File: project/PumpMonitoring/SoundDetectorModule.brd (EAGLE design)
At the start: 46 x 22 mm, 32 parts, among them CN1 JST-PH-K*, IC1 LMV324

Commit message: modify schematic of sound detect module.
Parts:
- added C5, C6: NC, SparkFun-Capacitors:1206
- added R22: NC, SparkFun-Resistors:0603-RES
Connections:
- new net N$13: C5.2
- net GND: now also C5.1, C6.1
- net N$2: now also C6.2, R22.2
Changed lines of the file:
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@@
 <?xml version="1.0" encoding="utf-8"?>
 <!DOCTYPE eagle SYSTEM "eagle.dtd">
-<eagle version="7.7.0">
+<eagle version="7.6.0">
 <drawing>
 <settings>
@@
 <layer number="21" name="tPlace" color="7" fill="1" visible="yes" active="yes"/>
 <layer number="22" name="bPlace" color="7" fill="1" visible="yes" active="yes"/>
-<layer number="23" name="tOrigins" color="15" fill="1" visible="no" active="yes"/>
-<layer number="24" name="bOrigins" color="15" fill="1" visible="no" active="yes"/>
+<layer number="23" name="tOrigins" color="15" fill="1" visible="yes" active="yes"/>
+<layer number="24" name="bOrigins" color="15" fill="1" visible="yes" active="yes"/>
 <layer number="25" name="tNames" color="7" fill="1" visible="no" active="yes"/>
 <layer number="26" name="bNames" color="7" fill="1" visible="no" active="yes"/>
@@
 <element name="R20" library="resistor" package="0207/7" value="0" x="12.319" y="6.731" rot="R180"/>
 <element name="R21" library="resistor" package="0207/7" value="0" x="30.226" y="6.858"/>
+<element name="C5" library="SparkFun-Capacitors" package="1206" value="NC" x="1.27" y="-3.81">
+<attribute name="PROD_ID" value="CAP-10057" x="1.27" y="-3.81" size="1.778" layer="27" display="off"/>
+</element>
+<element name="R22" library="SparkFun-Resistors" package="0603-RES" value="NC" x="1.27" y="-7.62">
+<attribute name="PROD_ID" value="RES-07856" x="1.27" y="-7.62" size="1.778" layer="27" display="off"/>
+</element>
+<element name="C6" library="SparkFun-Capacitors" package="1206" value="NC" x="1.27" y="-11.43">
+<attribute name="PROD_ID" value="CAP-10057" x="1.27" y="-11.43" size="1.778" layer="27" display="off"/>
+</element>
 </elements>
 <signals>
@@
 <wire x1="35.306" y1="13.973" x2="33.912" y2="15.367" width="0.2032" layer="1"/>
 <wire x1="33.912" y1="15.367" x2="33.147" y2="15.367" width="0.2032" layer="1"/>
+<contactref element="C5" pad="1"/>
+<contactref element="C6" pad="1"/>
+<wire x1="-0.13" y1="-3.81" x2="-0.13" y2="-11.43" width="0" layer="19" extent="1-1"/>
+<wire x1="7.461" y1="13.589" x2="-0.13" y2="-3.81" width="0" layer="19" extent="1-1"/>
 </signal>
 <signal name="N$2">
@@
 <wire x1="16.764" y1="9.525" x2="16.002" y2="8.763" width="0.2032" layer="1"/>
 <wire x1="16.002" y1="8.763" x2="12.7" y2="8.763" width="0.2032" layer="1"/>
+<contactref element="R22" pad="2"/>
+<contactref element="C6" pad="2"/>
+<wire x1="2.12" y1="-7.62" x2="12.7" y2="8.763" width="0" layer="19" extent="1-1"/>
+<wire x1="2.67" y1="-11.43" x2="2.12" y2="-7.62" width="0" layer="19" extent="1-1"/>
 </signal>
 <signal name="AUDIO">
@@
 <wire x1="21.883" y1="4.279" x2="20.701" y2="5.461" width="0.2032" layer="1"/>
 </signal>
+<signal name="N$13">
+<contactref element="C5" pad="2"/>
+</signal>
 </signals>

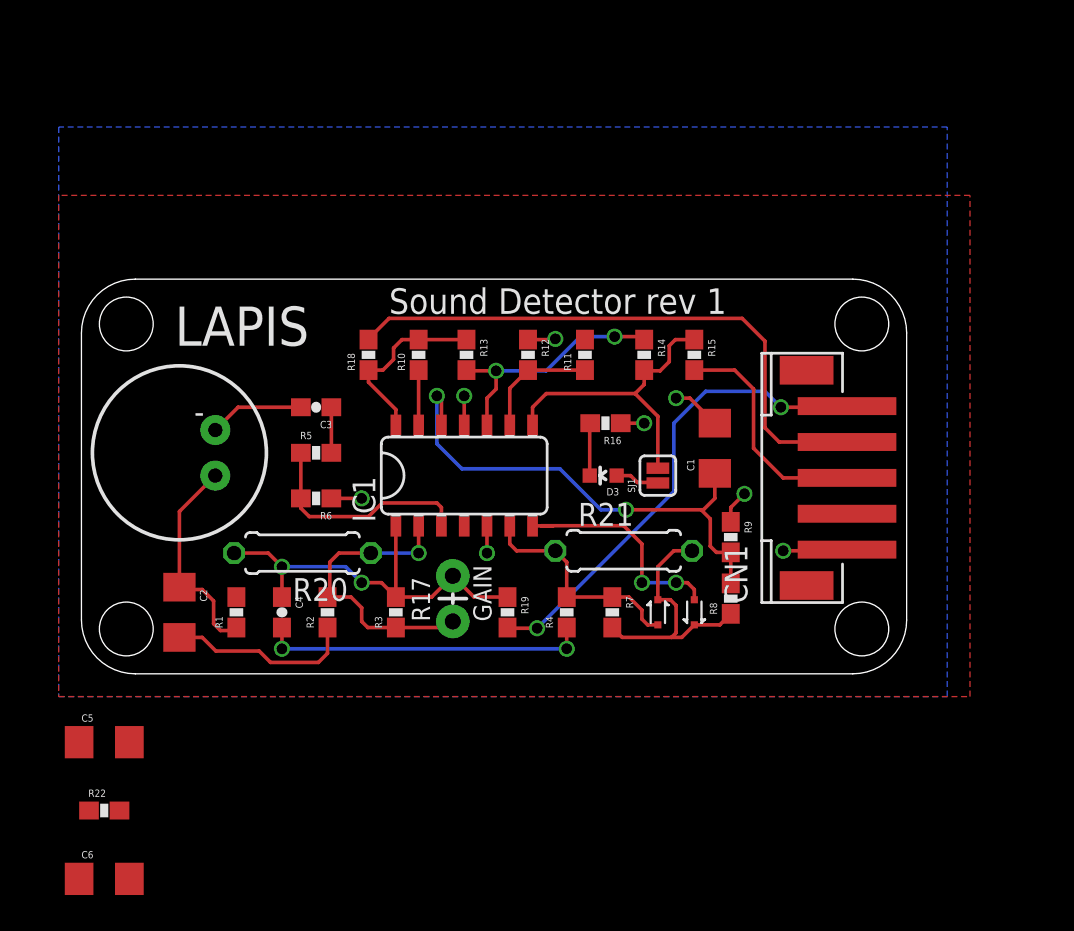
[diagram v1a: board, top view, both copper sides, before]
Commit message: update sound detector module
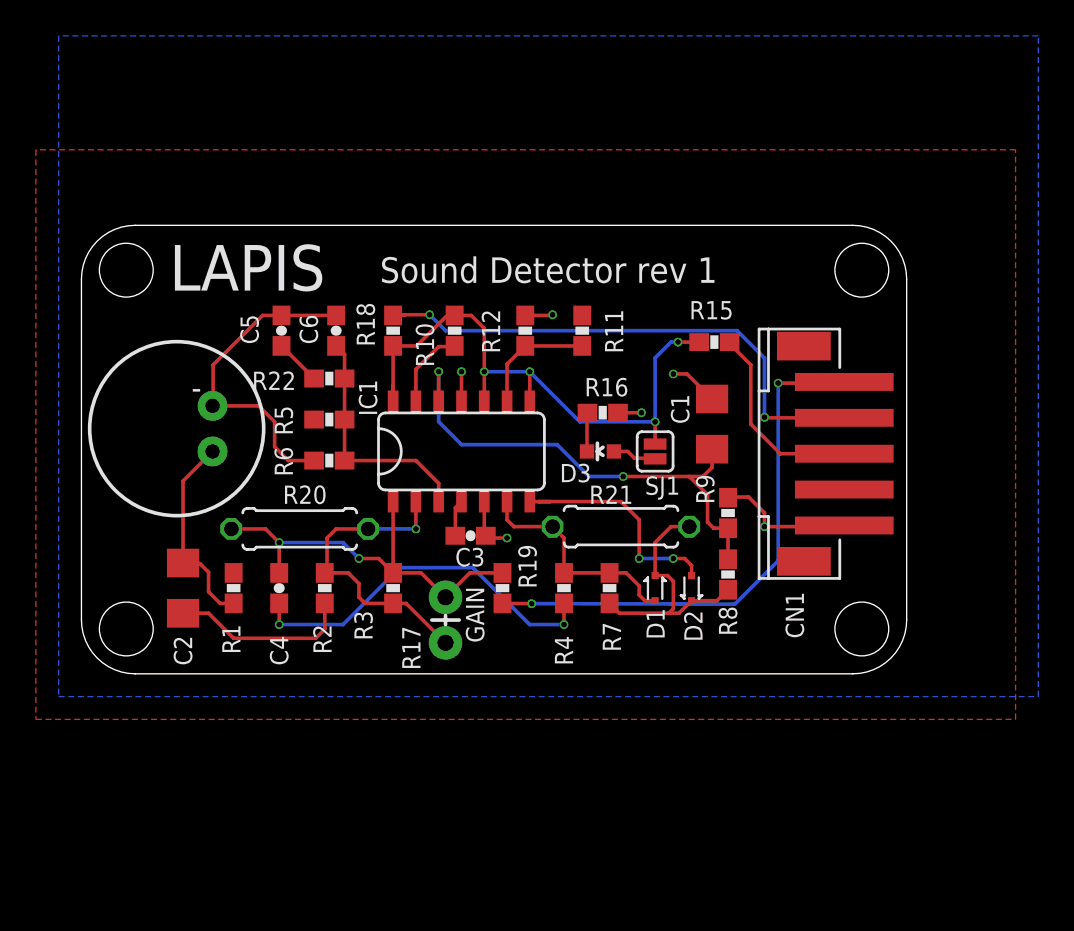
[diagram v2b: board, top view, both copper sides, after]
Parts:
- removed R13: 1K, SparkFun-Resistors:0603-RES
- removed R14: 100k, SparkFun-Resistors:0603-RES
- C5, C6: device SparkFun-Capacitors:1206 -> SparkFun-Capacitors:0603-CAP
- moved C6 33.2 mm to (14.2, 19.1), turned to 90 degrees
- moved R22 27.2 mm to (13.8, 16.5)
- moved C5 25.0 mm to (11.2, 19.1), turned to 270 degrees
- moved C3 11.2 mm to (21.7, 7.70), turned to 0 degrees
- moved R10 2.42 mm to (20.8, 19.1)
- moved R6 2.23 mm to (13.8, 11.9), turned to 0 degrees
- moved R5 2.00 mm to (13.8, 14.2), turned to 180 degrees
- moved R18 1.92 mm to (17.4, 19.1)
- moved R19 1.37 mm to (23.5, 4.78)
- moved C2 1.36 mm to (5.66, 4.78)
- moved D3 1.35 mm to (28.9, 12.4)
- moved IC1 1.35 mm to (20.5, 12.4)
- moved SJ1 1.35 mm to (32.0, 12.4)
- moved R21 1.35 mm to (30.1, 8.20)
- moved R8 1.35 mm to (36.0, 5.54)
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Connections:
- removed net N$16: IC1.10, R13.2, R14.1
- removed net N$17: IC1.8, R14.2, R15.1, SJ1.2
- net AMPENV: now also IC1.10, IC1.8, R15.1, SJ1.2; no longer R13.1
- net GND: now also C6.2; no longer C6.1
- net N$13: now also R22.1
- net N$2: now also C6.1; no longer C6.2
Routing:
- net AMPENV: track 10.2 -> 34.0 mm, vias 0 -> 4
- net N$17: track 17.7 -> 0.00 mm
- net GND: track 21.2 -> 36.1 mm, vias 8 -> 6
- net N$16: track 14.0 -> 0.00 mm, vias 2 -> 0
- net AUDIO: track 27.0 -> 30.0 mm
- net ENVELOPE: track 32.9 -> 30.1 mm, vias 0 -> 2
- net N$6: track 18.2 -> 20.9 mm
- net N$13: track 0.00 -> 2.57 mm
- net GATE: track 12.9 -> 11.0 mm
- net N$11: track 3.08 -> 4.47 mm
- net N$2: track 12.6 -> 13.4 mm
- net N$3: track 2.93 -> 2.17 mm
- net N$4: track 17.1 -> 17.6 mm
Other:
- board size 46 x 22 mm -> 46 x 25 mm
- board text added: "D1"
- board text added: "D2"

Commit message: add ti.lbr and update motion/sound module
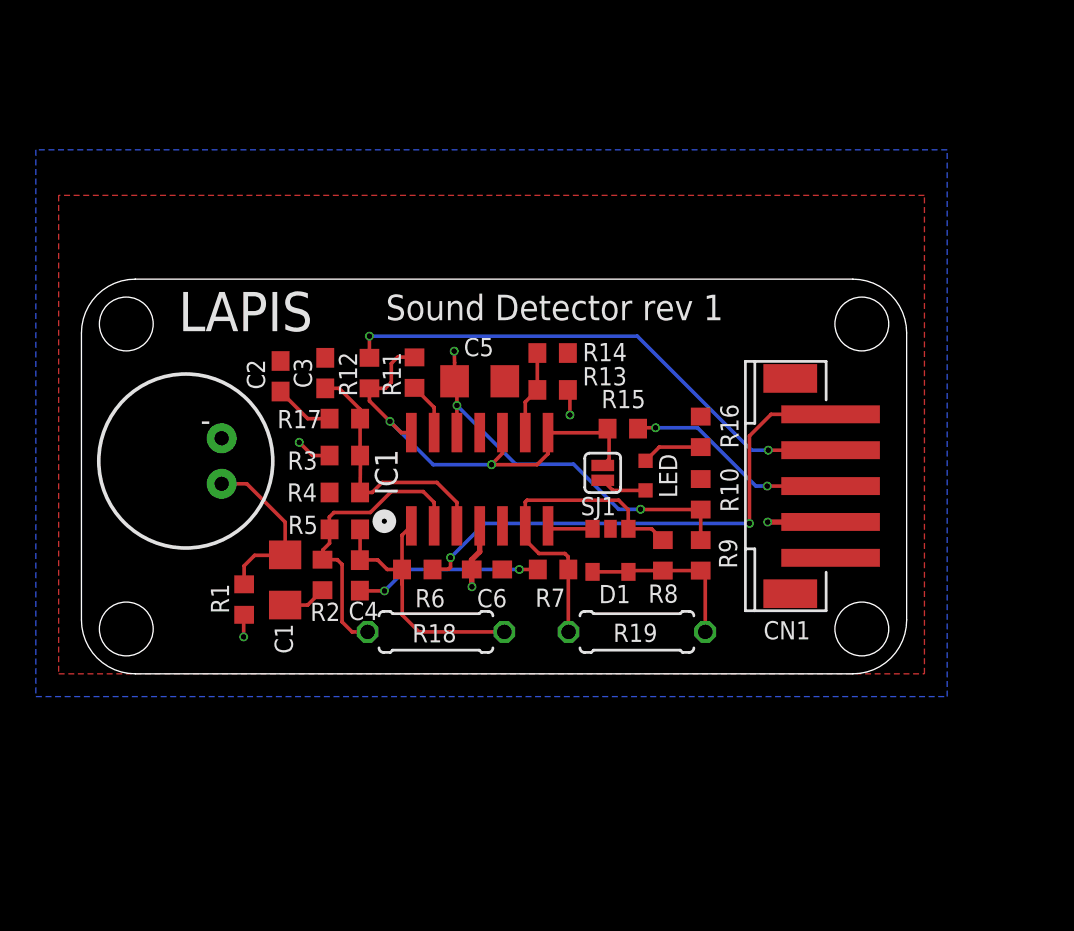
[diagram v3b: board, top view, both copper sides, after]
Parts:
- removed D2: RB751, SparkFun-DiscreteSemi:SOD-523
- removed D3: RED, SparkFun-LED:LED-0603
- removed R20, R21: 0, resistor:0207/7
- removed R22: NC, SparkFun-Resistors:0603-RES
- added LED: RED, lazurite:SML-E1X
- added R13: 100k, rcl:R0603
- added R14: 3.3k, rcl:R0603
- C1: device SparkFun-Capacitors:1206 -> rcl:C1206
- C2: value 10uF -> NC; device SparkFun-Capacitors:1206 -> rcl:C0603
- C3: value 1.0uF -> NC; device SparkFun-Capacitors:0603-CAP -> rcl:C0603
- C4: device SparkFun-Capacitors:0603-CAP -> rcl:C0603
- C5: value NC -> 10uF; device SparkFun-Capacitors:0603-CAP -> rcl:C1206
- C6: value NC -> 1.0uF; device SparkFun-Capacitors:0603-CAP -> rcl:C0603
- D1: value RB751 -> RRE04EA4D; device SparkFun-DiscreteSemi:SOD-523 -> rohm2:TSMD5
- IC1: device SparkFun-AnalogIC:SO014 -> ti:SO14
- R1, R15, R16, R2, R4: device SparkFun-Resistors:0603-RES -> rcl:R0603
- R10: value 1K -> 10K; device SparkFun-Resistors:0603-RES -> rcl:R0603
- R11: value 100k -> 1K; device SparkFun-Resistors:0603-RES -> rcl:R0603
- R12: value 3.3k -> 100; device SparkFun-Resistors:0603-RES -> rcl:R0603
- R17: value GAIN -> NC; device SparkFun-Resistors:AXIAL-0.1EZ -> rcl:R0603
- R18, R19: value 100 -> NC; device SparkFun-Resistors:0603-RES -> resistor:0207/7
- R3: value 100k -> 10K; device SparkFun-Resistors:0603-RES -> rcl:R0603
- R5: value 10K -> 100k; device SparkFun-Resistors:0603-RES -> rcl:R0603
- R6, R9: value 10K -> 100; device SparkFun-Resistors:0603-RES -> rcl:R0603
- R7: value 22K -> 10K; device SparkFun-Resistors:0603-RES -> rcl:R0603
- R8: value 100 -> 22K; device SparkFun-Resistors:0603-RES -> rcl:R0603
- moved C1 25.3 mm to (11.4, 5.23), turned to 270 degrees
- moved R18 17.0 mm to (19.8, 2.34), turned to 0 degrees
- moved R10 16.5 mm to (34.5, 10.0), turned to 270 degrees
- moved C6 15.7 mm to (22.6, 5.82), turned to 0 degrees
- moved R17 13.7 mm to (14.7, 14.2), turned to 0 degrees
- moved R4 13.3 mm to (14.7, 10.1), turned to 0 degrees
- moved C2 13.0 mm to (11.1, 16.6)
- moved C3 12.2 mm to (13.6, 16.8), turned to 90 degrees
- moved C5 11.4 mm to (22.2, 16.3), turned to 0 degrees
- moved R11 9.63 mm to (18.6, 16.8)
- moved R12 9.00 mm to (16.1, 16.8), turned to 90 degrees
- moved R19 7.88 mm to (31.0, 2.34), turned to 0 degrees
- moved R3 7.87 mm to (14.7, 12.2), turned to 180 degrees
- moved R6 7.80 mm to (18.7, 5.82)
- moved R15 7.03 mm to (30.2, 13.7)
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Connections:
- net AMPENV: now also R11.2, R12.1; no longer R10.2, R18.1
- net AUDIO: now also R6.2; no longer R19.2
- net ENVELOPE: now also R12.2; no longer R18.2
- net GND: now also C2.1, C5.2, R10.1, R14.1, R4.1; no longer C1.2, C5.1, R12.1, R6.1, R9.1
- net N$: now also R18.2, R5.2, R6.1; no longer R17.P$2, R19.1, R20.2, R3.2
- net N$1: now also C1.1; no longer C2.1
- net N$10: now also C5.1, R10.2; no longer C1.1, R8.2
- net N$11: now also R11.1; no longer R10.1
- net N$12: now also LED.A; no longer D3.A
- net N$13: now also C2.2, R17.1; no longer C5.2, R22.1
- net N$15: now also R13.1, R14.2; no longer R11.1, R12.2
- net N$2: now also C3.1, R17.2, R3.1, R4.2; no longer C6.1, R22.2, R5.1, R6.2
- net N$3: now also LED.C; no longer D3.C
- net N$4: now also R18.1, R5.1; no longer R17.P$1, R20.1, R3.1
- net N$5: now also C1.2; no longer C2.2
- net N$6: now also R7.1; no longer R4.1
- net N$7: now also D1.1, R19.1, R7.2, R8.1; no longer D1.A, R21.1, R4.2, R7.1
- net N$8: now also D1.3; no longer D2.A
- net N$9: now also D1.4, D1.5, R19.2, R8.2, R9.1; no longer D1.C, D2.C, R21.2, R7.2, R8.1
- net VCC: now also C6.1, R13.2, R3.2; no longer C3.1, R11.2, R5.2
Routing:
- net GND: track 36.1 -> 0.00 mm, vias 6 -> 0
- net N$6: track 20.9 -> 10.4 mm
- net N$8: track 13.0 -> 2.55 mm, vias 2 -> 0
- net VCC: track 2.04 -> 12.2 mm, vias 0 -> 5
- net N$5: track 10.1 -> 2.43 mm
- net AMPENV: track 34.0 -> 26.6 mm, vias 4 -> 2
- net N$: track 23.1 -> 16.4 mm, vias 2 -> 0
- net N$7: track 12.6 -> 18.3 mm
- net N$10: track 28.1 -> 22.8 mm, vias 2 -> 3
- net N$9: track 14.5 -> 9.90 mm
- net N$1: track 11.8 -> 9.82 mm
- net N$15: track 6.68 -> 4.71 mm
- net N$11: track 4.47 -> 2.95 mm
- net N$3: track 2.17 -> 3.39 mm
- net GATE: track 11.0 -> 12.1 mm, vias 0 -> 2
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- added copper zone on layer 1, net GND
- added copper zone on layer 16, net VCC
- removed copper zone on layer 16, net GND
- removed copper zone on layer 1, net VCC
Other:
- board size 46 x 25 mm -> 46 x 22 mm
- board text removed: "D1"
- board text removed: "D2"

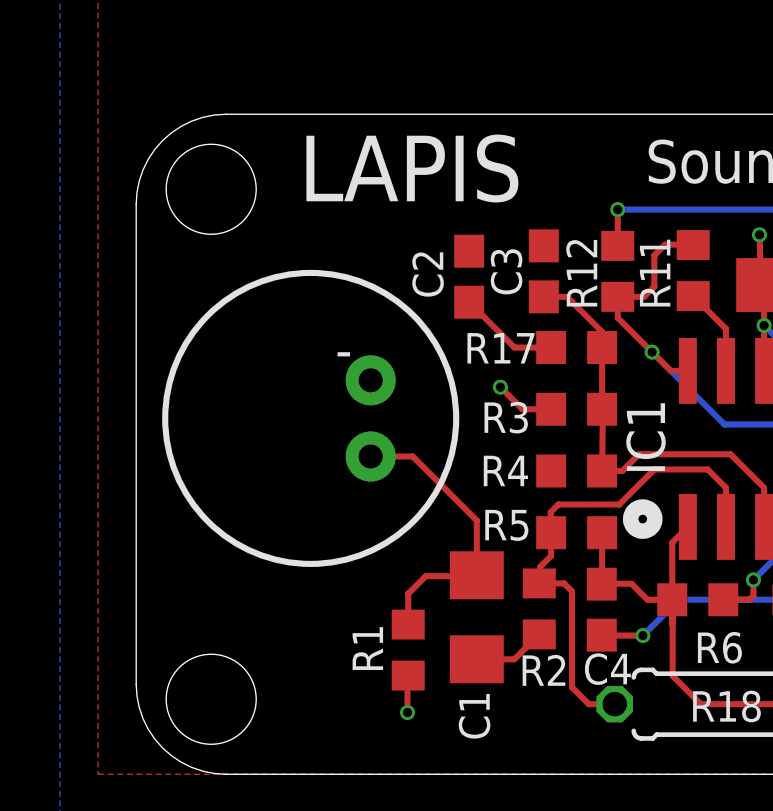
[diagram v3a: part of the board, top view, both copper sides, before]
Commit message: update project of pump monitoring incl. sound and motion.
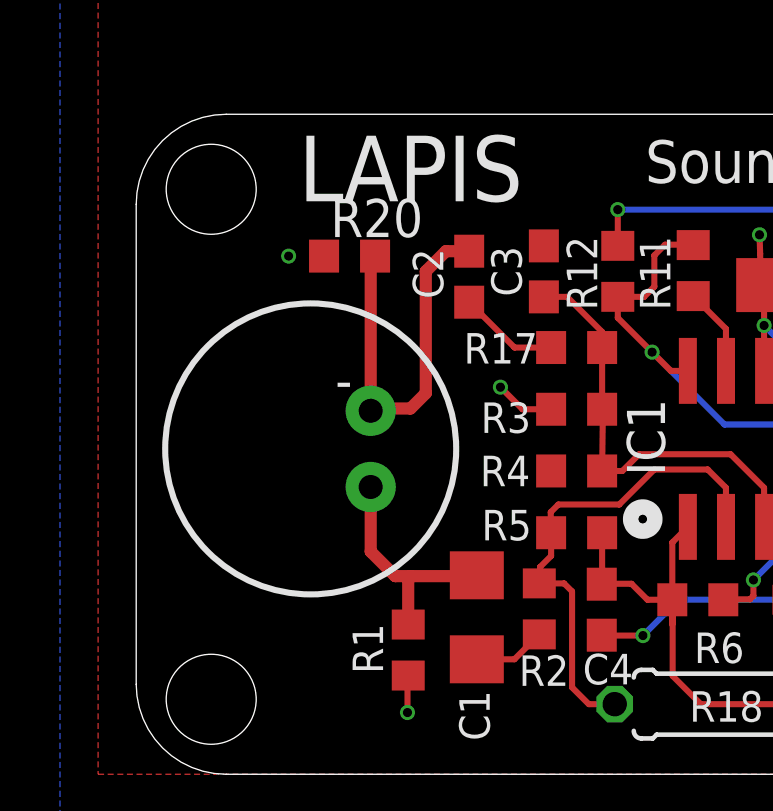
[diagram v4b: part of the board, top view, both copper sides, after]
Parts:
- added R20: 0, rcl:R0603
- moved MIC1 1.02 mm to (5.82, 10.8)
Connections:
- new net N$14: C2.1, MIC1.2, R20.2
- net GND: now also R20.1; no longer C2.1, MIC1.2
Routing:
- net N$14: track 0.00 -> 13.1 mm
- net N$1: track 9.82 -> 7.69 mm
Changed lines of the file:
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@@
 <?xml version="1.0" encoding="utf-8"?>
 <!DOCTYPE eagle SYSTEM "eagle.dtd">
-<eagle version="7.7.0">
+<eagle version="7.6.0">
 <drawing>
 <settings>
@@
 <layer number="21" name="tPlace" color="7" fill="1" visible="yes" active="yes"/>
 <layer number="22" name="bPlace" color="7" fill="1" visible="yes" active="yes"/>
-<layer number="23" name="tOrigins" color="15" fill="1" visible="no" active="yes"/>
-<layer number="24" name="bOrigins" color="15" fill="1" visible="no" active="yes"/>
+<layer number="23" name="tOrigins" color="15" fill="1" visible="yes" active="yes"/>
+<layer number="24" name="bOrigins" color="15" fill="1" visible="yes" active="yes"/>
 <layer number="25" name="tNames" color="7" fill="1" visible="no" active="yes"/>
 <layer number="26" name="bNames" color="7" fill="1" visible="no" active="yes"/>
@@
 <attribute name="NAME" x="33.2105" y="9.8044" size="1.016" layer="21" font="vector" ratio="15" rot="R90"/>
 </element>
-<element name="MIC1" library="SparkFun-Sensors" package="MIC-9.7MM" value="MIC9.7MM" x="5.8166" y="11.8618" smashed="yes" rot="R180">
-<attribute name="PROD_ID" value="COMP-08856" x="5.8166" y="11.8618" size="1.778" layer="27" rot="R180" display="off"/>
+<element name="MIC1" library="SparkFun-Sensors" package="MIC-9.7MM" value="MIC9.7MM" x="5.8166" y="10.8458" smashed="yes" rot="R180">
+<attribute name="PROD_ID" value="COMP-08856" x="5.8166" y="10.8458" size="1.778" layer="27" rot="R180" display="off"/>
 </element>
 <element name="R1" library="rcl" package="R0603" value="2.2k" x="9.0678" y="4.1402" smashed="yes" rot="R270">
@@
 <attribute name="VALUE" x="28.0416" y="8.9408" size="1.27" layer="27" rot="R90"/>
 </element>
+<element name="R20" library="rcl" package="R0603" value="0" x="7.112" y="17.272"/>
 </elements>
 <signals>
@@
 <contactref element="C1" pad="1"/>
 <contactref element="MIC1" pad="1"/>
-<wire x1="11.3538" y1="6.6324" x2="11.3538" y2="8.4582" width="0.2032" layer="1"/>
-<wire x1="11.3538" y1="8.4582" x2="9.2202" y2="10.5918" width="0.2032" layer="1"/>
-<wire x1="9.2202" y1="10.5918" x2="7.8166" y2="10.5918" width="0.2032" layer="1"/>
-<wire x1="9.0678" y1="4.9902" x2="9.0678" y2="6.0198" width="0.2032" layer="1"/>
-<wire x1="9.0678" y1="6.0198" x2="9.652" y2="6.604" width="0.2032" layer="1"/>
-<wire x1="9.652" y1="6.604" x2="11.3254" y2="6.604" width="0.2032" layer="1"/>
-<wire x1="11.3254" y1="6.604" x2="11.3538" y2="6.6324" width="0.2032" layer="1"/>
+<wire x1="7.8166" y1="9.5758" x2="7.8166" y2="7.4234" width="0.4064" layer="1"/>
+<wire x1="7.8166" y1="7.4234" x2="8.636" y2="6.604" width="0.4064" layer="1"/>
+<wire x1="8.636" y1="6.604" x2="9.144" y2="6.604" width="0.4064" layer="1"/>
+<wire x1="9.144" y1="6.604" x2="11.3254" y2="6.604" width="0.4064" layer="1"/>
+<wire x1="11.3254" y1="6.604" x2="11.3538" y2="6.6324" width="0.4064" layer="1"/>
+<wire x1="9.0678" y1="4.9902" x2="9.0678" y2="6.5278" width="0.4064" layer="1"/>
+<wire x1="9.0678" y1="6.5278" x2="9.144" y2="6.604" width="0.4064" layer="1"/>
 </signal>
 <signal name="GND">
 <contactref element="CN1" pad="1"/>
 <contactref element="R4" pad="1"/>
-<contactref element="MIC1" pad="2"/>
 <contactref element="C5" pad="2"/>
 <contactref element="R10" pad="1"/>
@@
 <contactref element="R14" pad="1"/>
 <contactref element="R16" pad="1"/>
-<contactref element="C2" pad="1"/>
 <contactref element="C3" pad="2"/>
 <polygon width="0.4064" layer="1">
@@
 <contactref element="IC1" pad="5"/>
 <contactref element="IC1" pad="11"/>
+<contactref element="R20" pad="1"/>
+<via x="5.08" y="17.272" extent="1-16" drill="0.3"/>
 </signal>
 <signal name="N$2">
@@
 <wire x1="26.172" y1="8.0834" x2="26.0096" y2="8.2458" width="0.2032" layer="1"/>
 </signal>
+<signal name="N$14">
+<contactref element="MIC1" pad="2"/>
+<contactref element="C2" pad="1"/>
+<contactref element="R20" pad="2"/>
+<wire x1="11.0998" y1="17.4362" x2="10.3242" y2="17.4362" width="0.4064" layer="1"/>
+<wire x1="10.3242" y1="17.4362" x2="9.652" y2="16.764" width="0.4064" layer="1"/>
+<wire x1="9.652" y1="16.764" x2="9.652" y2="12.7" width="0.4064" layer="1"/>
+<wire x1="9.652" y1="12.7" x2="9.144" y2="12.192" width="0.4064" layer="1"/>
+<wire x1="9.144" y1="12.192" x2="7.8928" y2="12.192" width="0.4064" layer="1"/>
+<wire x1="7.8928" y1="12.192" x2="7.8166" y2="12.1158" width="0.4064" layer="1"/>
+<wire x1="7.8166" y1="12.1158" x2="7.8166" y2="17.1266" width="0.4064" layer="1"/>
+<wire x1="7.8166" y1="17.1266" x2="7.962" y2="17.272" width="0.4064" layer="1"/>
+</signal>
 </signals>
